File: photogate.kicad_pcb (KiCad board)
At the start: 2 copper layers, 50 x 30 mm, 22 parts, among them P1 CONN_01X02, P10 CONN_01X01, P11 CONN_01X01, P2 CONN_01X02, P3 CONN_01X01, P4 CONN_02X05, P5 CONN_02X04, P6 CONN_01X02, P7 CONN_02X05, P8 CONN_01X02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

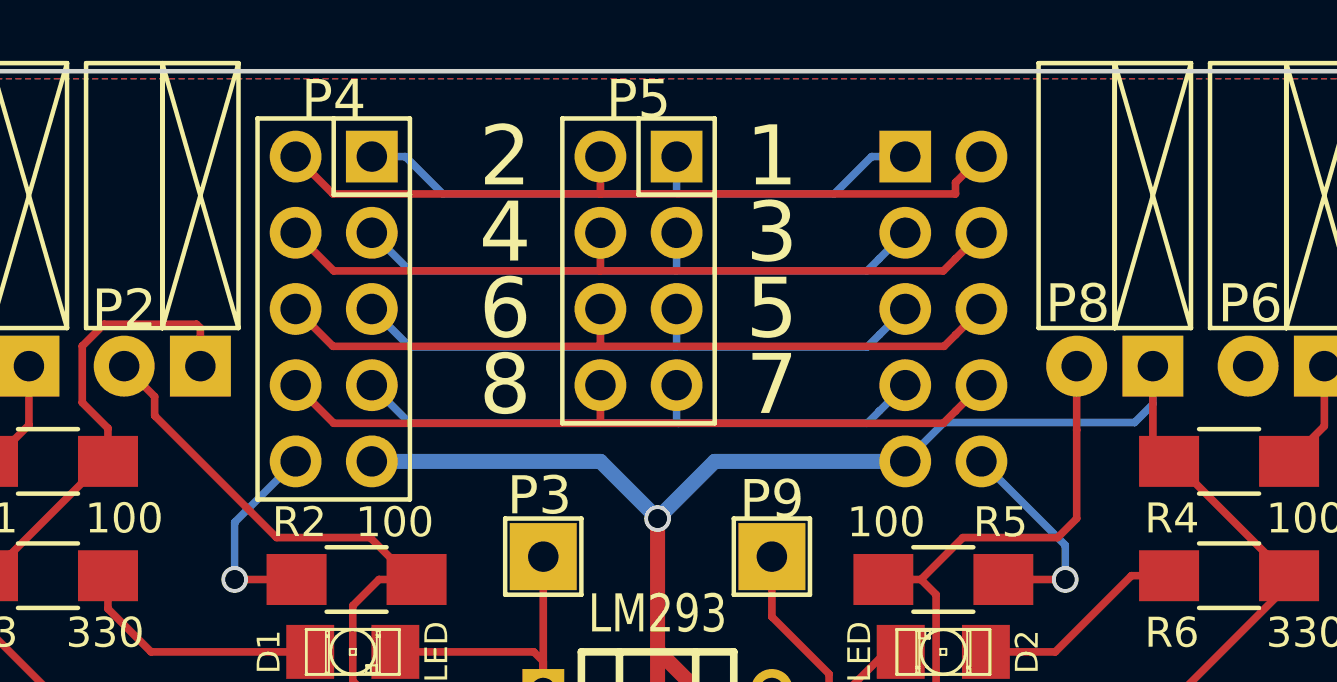
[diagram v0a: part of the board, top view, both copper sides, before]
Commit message: Flipped flat cable connector
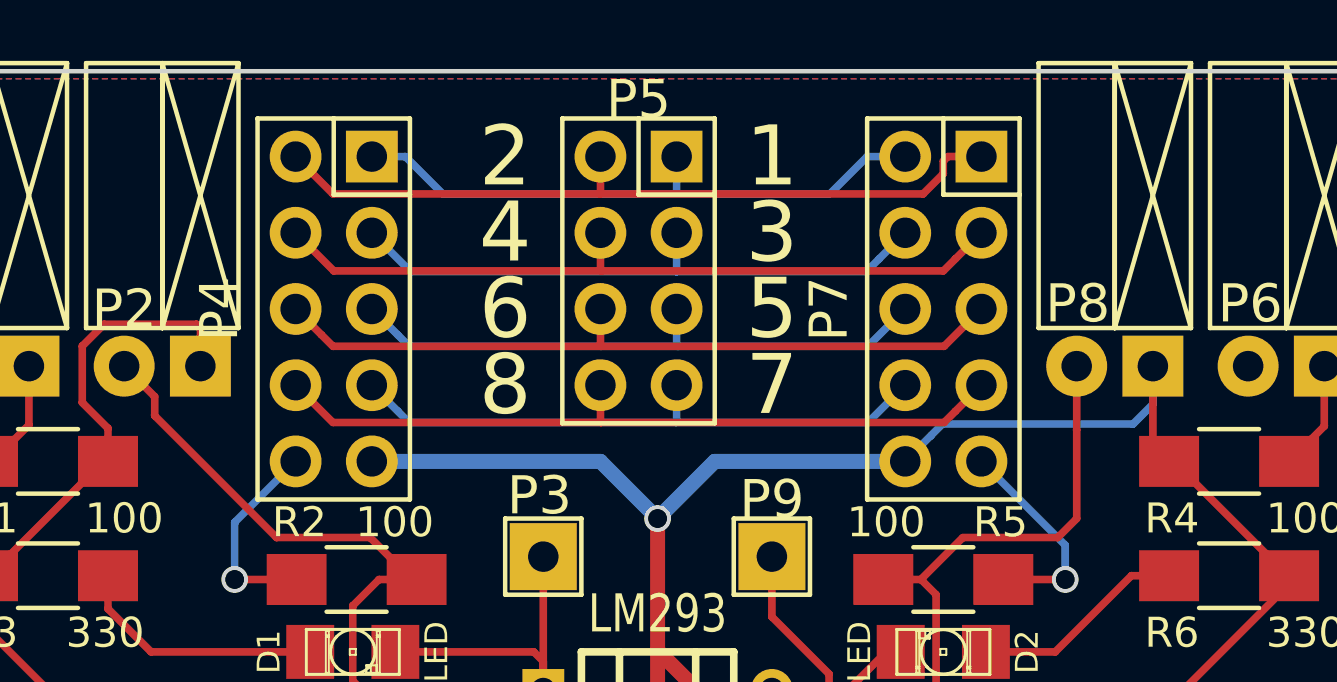
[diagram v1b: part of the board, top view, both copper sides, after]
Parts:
- P7: moved to F.Cu
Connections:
- P7 pad 1: D1 -> D2
- P7 pad 10: GND -> +5V
- P7 pad 2: D2 -> D1
- P7 pad 3: D3 -> D4
- P7 pad 4: D4 -> D3
- P7 pad 5: D5 -> D6
- P7 pad 6: D6 -> D5
- P7 pad 7: D7 -> D8
- P7 pad 8: D8 -> D7
- P7 pad 9: +5V -> GND

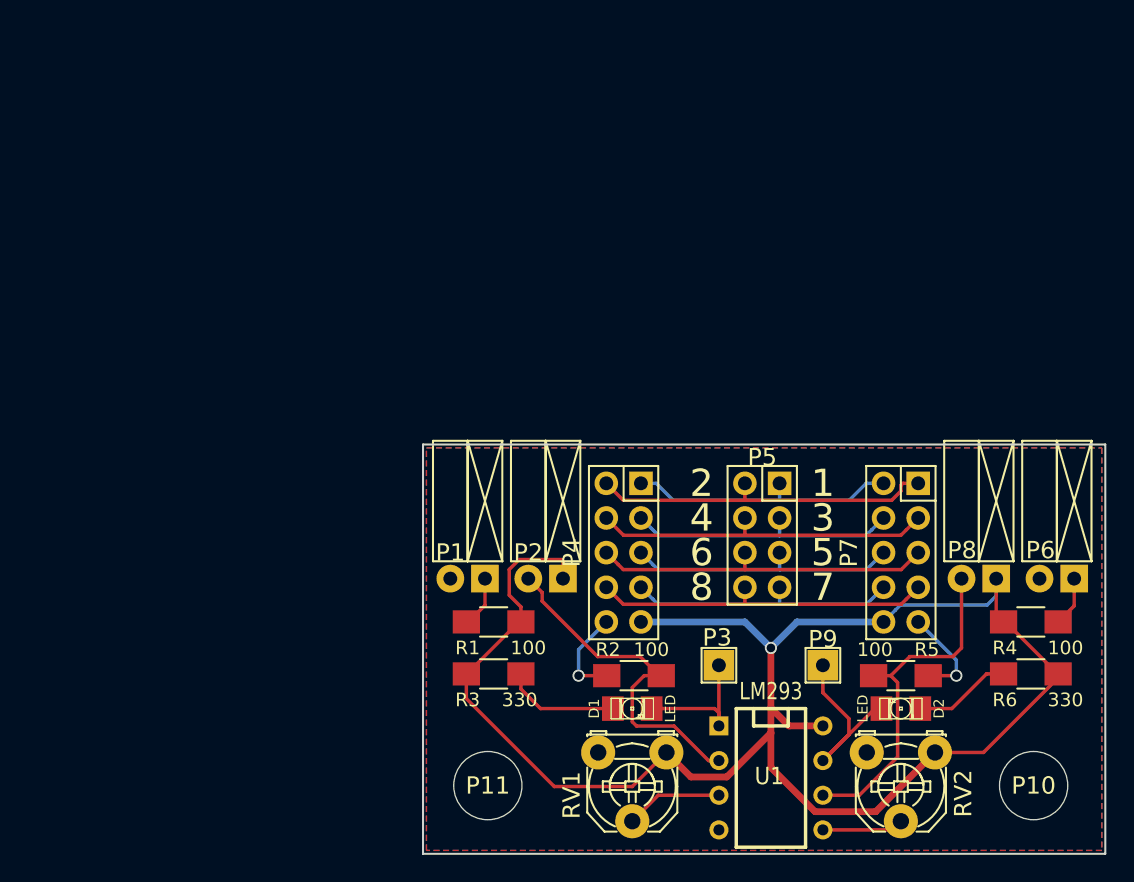
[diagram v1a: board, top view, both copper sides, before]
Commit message: Rebuild layout w/ updated footprints
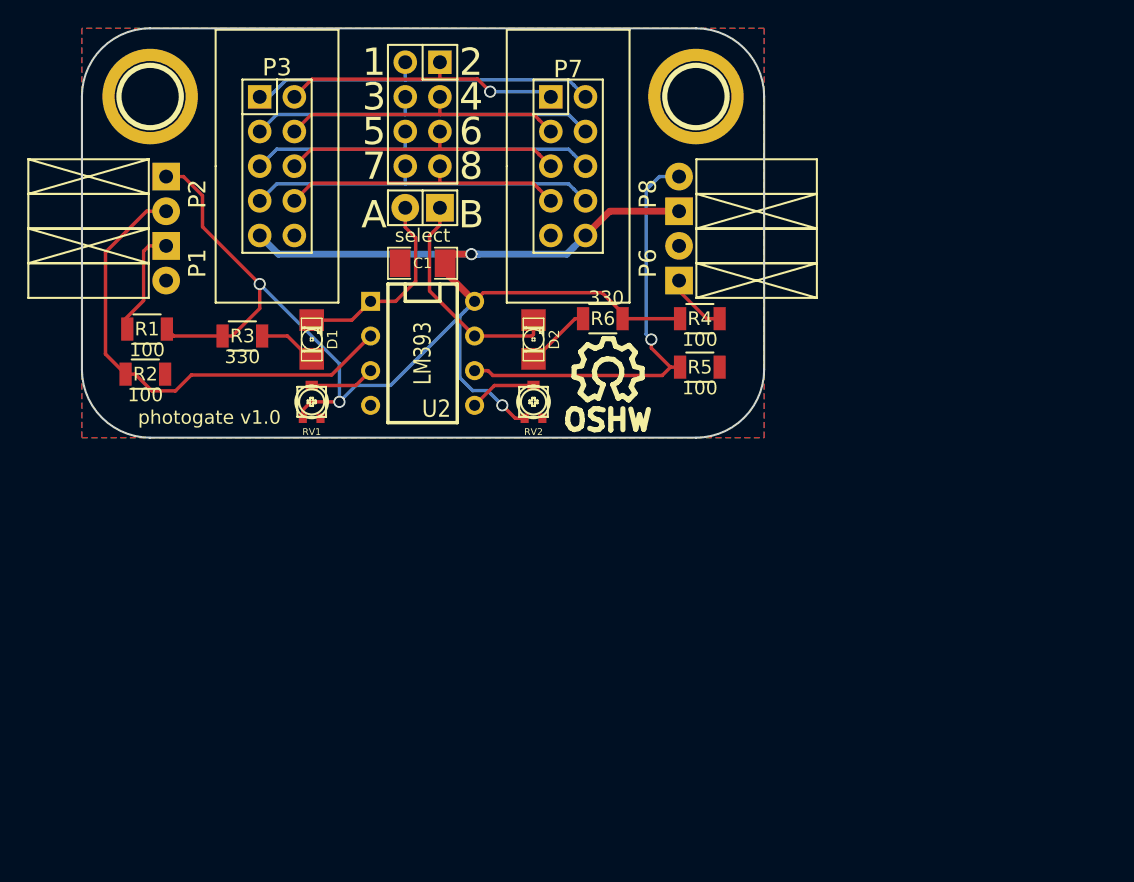
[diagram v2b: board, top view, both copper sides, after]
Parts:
- removed P10, P11: CONN_01X01, Mounting_Holes:MountingHole_5mm
- removed P9: CONN_01X01, Socket_Strips:Socket_Strip_Straight_1x01
- removed U1: LM293, Sockets_DIP:DIP-8__300
- added 1PIN: P***, Connect:1pin, F.Cu at (145.0, 65.0)
- added 1PIN: P***, Connect:1pin, F.Cu at (105.0, 65.0)
- added C1: 100nF, SMD_Packages:SMD-1206, F.Cu at (125.0, 77.2)
- added SYM: Symbol_OSHW-Logo_SilkScreen_07Jul2012, Symbols:Symbol_OSHW-Logo_SilkScreen, F.Cu at (138.6, 85.2)
- added U2: LM393, Sockets_DIP:DIP-8__300, F.Cu at (125.0, 83.8)
- P3: value CONN_01X01 -> CONN_02X05; footprint Socket_Strips:Socket_Strip_Straight_1x01 -> photogate_mods:Wurth_2x05_HEADER_STRAIGHT
- P4: value CONN_02X05 -> CONN_02X04; footprint Socket_Strips:Socket_Strip_Straight_2x05 -> Socket_Strips:Socket_Strip_Straight_2x04
- P5: value CONN_02X04 -> CONN_01X02; footprint Socket_Strips:Socket_Strip_Straight_2x04 -> Socket_Strips:Socket_Strip_Straight_1x02
- P7: footprint Socket_Strips:Socket_Strip_Straight_2x05 -> photogate_mods:Wurth_2x05_HEADER_STRAIGHT
- R1, R2, R3, R4, R5, R6: footprint Resistors_SMD:R_1206_HandSoldering -> Resistors_SMD:R_1206
- RV1, RV2: footprint Potentiometers:Potentiometer_Triwood_RM-065 -> photogate_mods:PVZ2A
- moved P3 48.9 mm to (114.3, 70.1)
- moved R2 42.1 mm to (104.6, 85.3), turned to 0 degrees
- moved R6 40.8 mm to (138.2, 81.3)
- moved P2 39.6 mm to (106.2, 72.1), turned to 90 degrees
- moved RV2 39.0 mm to (133.1, 87.4), turned to 0 degrees
- moved D2 38.2 mm to (133.1, 82.8), turned to 90 degrees
- moved P7 37.4 mm to (135.6, 70.1), turned to 270 degrees
- moved RV1 36.7 mm to (116.8, 87.4), turned to 0 degrees
- moved P6 36.1 mm to (143.8, 77.2), turned to 270 degrees
- moved D1 35.8 mm to (116.8, 82.8), turned to 90 degrees
- moved P8 35.7 mm to (143.8, 72.1), turned to 270 degrees
- moved P4 35.3 mm to (125.0, 66.3)
- moved P5 34.6 mm to (125.0, 73.2), turned to 0 degrees
- moved R1 33.3 mm to (104.8, 82.0)
- moved R4 32.9 mm to (145.3, 81.3)
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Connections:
- P3 pad 1: Vout1 -> D1
- P4 pad 1: D1 -> D2
- P4 pad 2: D2 -> D1
- P4 pad 3: D3 -> D4
- P4 pad 4: D4 -> D3
- P4 pad 5: D5 -> D6
- P4 pad 6: D6 -> D5
- P4 pad 7: D7 -> D8
- P4 pad 8: D8 -> D7
- P5 pad 1: D1 -> Vout2
- P5 pad 2: D2 -> Vout1
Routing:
- net GND: track 14.0 -> 0.00 mm, vias 2 -> 0
- net Net-(P2-Pad2): track 25.6 -> 35.4 mm
- net +5V: track 124.8 -> 115.7 mm, vias 1 -> 4
- net Net-(P8-Pad2): track 25.3 -> 32.0 mm, vias 0 -> 1
- net D1: track 20.1 -> 26.2 mm
- net D7: track 20.1 -> 26.2 mm
- net D5: track 20.1 -> 26.2 mm
- net D3: track 20.2 -> 26.2 mm
- net D2: track 25.4 -> 21.1 mm, vias 0 -> 1
- net Net-(D1-Pad1): track 8.44 -> 4.32 mm
- net D4: track 25.2 -> 21.1 mm
- net Vout1: track 10.5 -> 14.5 mm
- net D8: track 25.1 -> 21.1 mm
- net D6: track 25.1 -> 21.1 mm
- net Net-(P1-Pad1): track 3.83 -> 7.31 mm
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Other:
- outline, holes or cut-outs redrawn
- board text added: "A"
- board text added: "B"
- board text added: "photogate v1.0"
- board text added: "select"
